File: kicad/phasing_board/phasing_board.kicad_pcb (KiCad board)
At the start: 4 copper layers, 103.2 x 30 mm, 4 parts, among them J1 EdgeLaunch_SMA_BNC_F_1.6mm, P1 PhasingTab_TAB1, P2 PhasingTab_TAB2

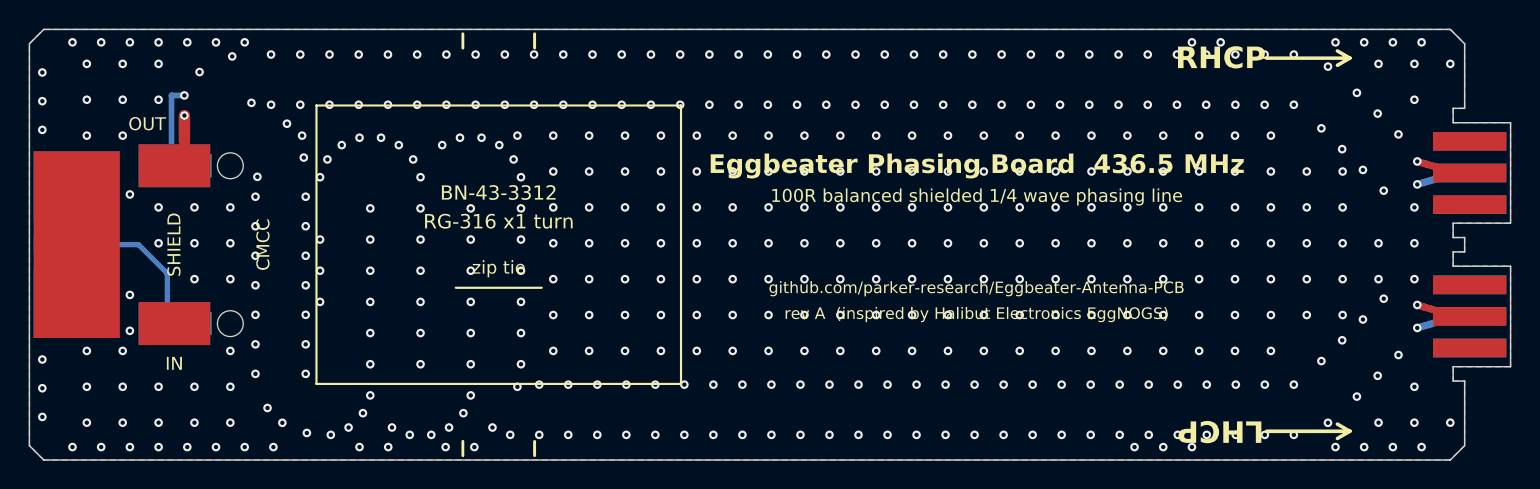
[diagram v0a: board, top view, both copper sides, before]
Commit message: chore: Make PCB smaller than 100mm for JLC cost
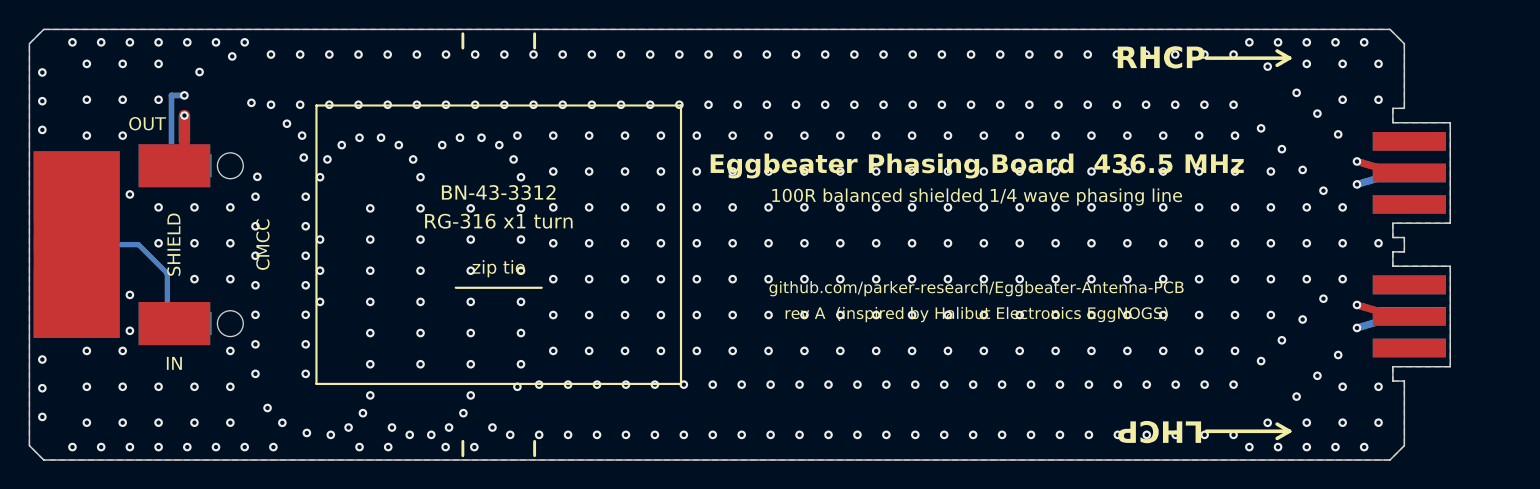
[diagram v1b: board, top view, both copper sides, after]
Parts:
- moved P1 4.20 mm to (145.8, 95.0)
- moved P2 4.20 mm to (145.8, 105.0)
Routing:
- net LINE_P: track 264.1 -> 255.7 mm
- net LINE_N: track 268.1 -> 259.7 mm
- net GND: vias 461 -> 442
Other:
- board size 103.2 x 30 mm -> 99 x 30 mm
